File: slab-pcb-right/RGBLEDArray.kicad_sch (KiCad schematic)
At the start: 60 parts

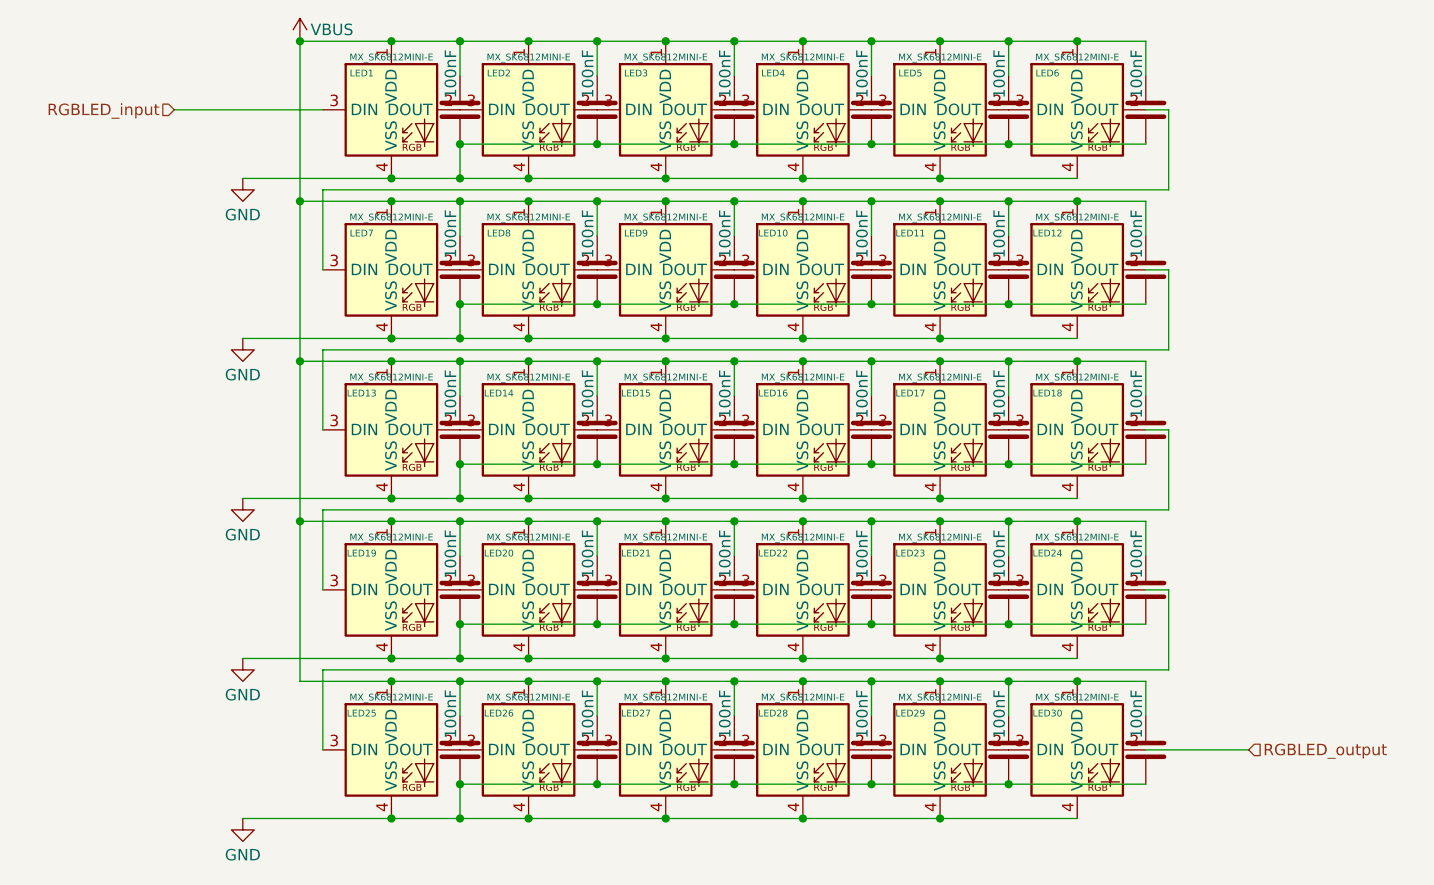
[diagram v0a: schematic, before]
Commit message: feat: route most of slab-pcb-right
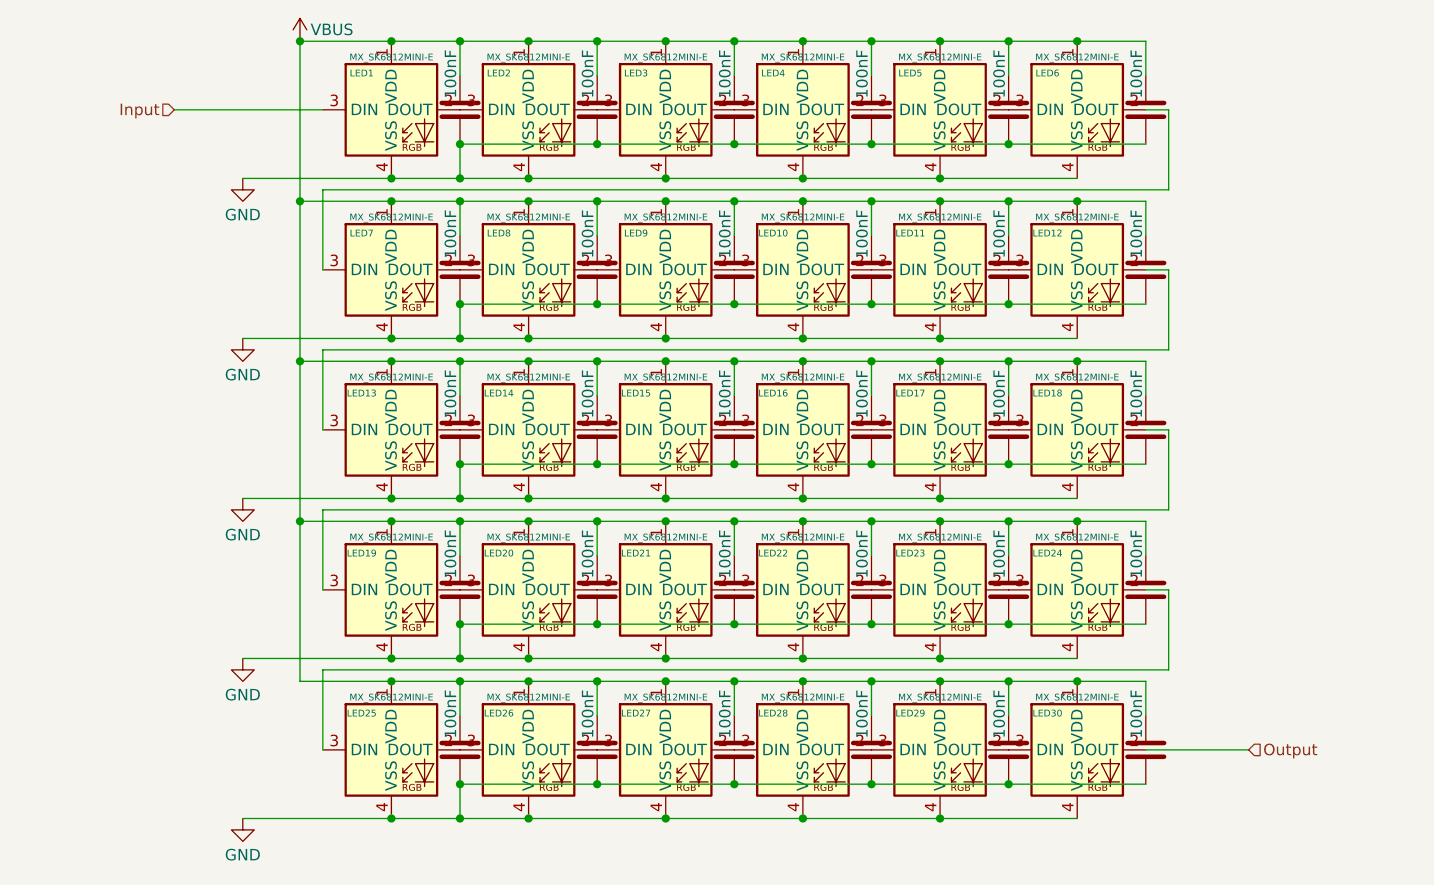
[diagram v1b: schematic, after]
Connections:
- net RGBLED_input renamed Input
- net RGBLED_output renamed Output
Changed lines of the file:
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@@
 		)
 	)
-	(hierarchical_label "RGBLED_input"
+	(hierarchical_label "Input"
 		(shape input)
 		(at 82.55 53.34 180)
@@
 		)
 	)
-	(hierarchical_label "RGBLED_output"
+	(hierarchical_label "Output"
 		(shape input)
 		(at 201.93 124.46 0)
